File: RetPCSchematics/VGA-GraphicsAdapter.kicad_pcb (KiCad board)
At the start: 2 copper layers, 183.4 x 101.3 mm, 45 parts, among them J1 Bus_ISA_8bit, J2 74320-9004, U1 74AUC2G125, U10 ATmega644P-20PU, U11 628128, U12 628128, U13 SN74LVC245AN, U14 74LS245, U15 74LVC2G240, U16 74LVC2G240, U17 74LVC1G18, U18 74LVC1G18, U19 74LVC1G18, U2 74LVC2G240, U20 74LVC1G18, U21 ATF22V10D, U22 74LS245, U23 74LVC1G373, U24 74LVC1G373, U25 74LVC1G373, U26 74LVC1G373, U27 74LVC1G373, U28 74LVC1G373, U29 74LVC1G373, U3 ATF22V10D, U30 74LVC1G373, U31 74LVC1G373, U32 74LVC1G373, U33 74LVC1G373, U34 74LVC1G373, U37 ATF22V10D, U4 ATF22V10D, U5 74LS245, U6 ATF22V10D, U7 74LS245, U8 74LS245, U9 74LS245, X1 DGOF5S3

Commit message: sync
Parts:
- removed R1: 4.7k, Resistor_THT:R_Axial_DIN0411_L9.9mm_D3.6mm_P5.08mm_Vertical
- removed R2, R3, R4, R5, R6, R7: 4.7k, Resistor_THT:R_Axial_DIN0411_L9.9mm_D3.6mm_P7.62mm_Vertical
- added RN1: R_Network08, Resistor_THT:R_Array_SIP9, F.Cu at (153.2, 62.5)
- added U36: TFP410, retsmd:HQFP-64_10x10mm_Pitch0.5mm_handsoldering, F.Cu at (225.0, 84.6)
- U11, U12: footprint Package_DIP:DIP-24_W7.62mm_Socket -> SMD_Packages:SOJ-32
- U37: value ATF22V10D -> ATF750C
- moved U28 338.2 mm to (55.5, 20.9)
- moved U29 338.2 mm to (55.5, 13.6)
- moved U30 338.2 mm to (55.5, 17.3)
- moved U19 328.7 mm to (69.8, 22.4)
- moved U2 328.7 mm to (69.6, 25.5)
- moved U20 328.7 mm to (64.9, 26.1)
- moved U24 328.7 mm to (64.9, 22.5)
- moved U26 326.2 mm to (77.3, 9.75)
- moved U31 326.2 mm to (77.3, 13.4)
- moved U33 326.2 mm to (77.3, 20.7)
- moved U34 326.2 mm to (77.3, 17.0)
- moved U23 321.3 mm to (55.6, 27.9)
- moved U25 315.6 mm to (45.2, 29.0)
- moved U5 265.5 mm to (87.4, 78.7)
- moved U13 172.7 mm to (186.7, 13.5)
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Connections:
- U7 pad 2: /A15 -> /A8
- U7 pad 3: /A14 -> /A9
- U7 pad 4: /A13 -> /A10
- U7 pad 5: /A12 -> /A11
- U7 pad 6: /A11 -> /A12
- U7 pad 7: /A10 -> /A13
- U7 pad 8: /A9 -> /A14
- U7 pad 9: /A8 -> /A15
- U9 pad 2: /A7 -> /A0
- U9 pad 3: /A6 -> /A0
- U9 pad 4: /A5 -> /A0
- U9 pad 7: /A0 -> /A5
- U9 pad 8: /A0 -> /A6
- U9 pad 9: /A0 -> /A7
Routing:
- net (no net): track 423.5 -> 0.00 mm, vias 16 -> 0
- net /A0: track 0.00 -> 314.4 mm, vias 0 -> 6
- net /A6: track 0.00 -> 64.5 mm, vias 0 -> 1
- net /A8: track 0.00 -> 63.0 mm, vias 0 -> 1
- net /A5: track 0.00 -> 60.8 mm, vias 0 -> 1
- net /A7: track 0.00 -> 60.2 mm, vias 0 -> 1
- net /A9: track 0.00 -> 45.9 mm
- net /A13: track 0.00 -> 45.9 mm
- net /A12: track 0.00 -> 45.9 mm
- net /A10: track 0.00 -> 45.9 mm
- net /A11: track 0.00 -> 45.9 mm
- net /A14: track 0.00 -> 45.7 mm
- net /A15: track 0.00 -> 45.7 mm
- net Net-(U10-Pad15): track 0.00 -> 38.4 mm
- net Net-(U10-Pad16): track 0.00 -> 37.8 mm
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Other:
- board text removed: "VRAM"

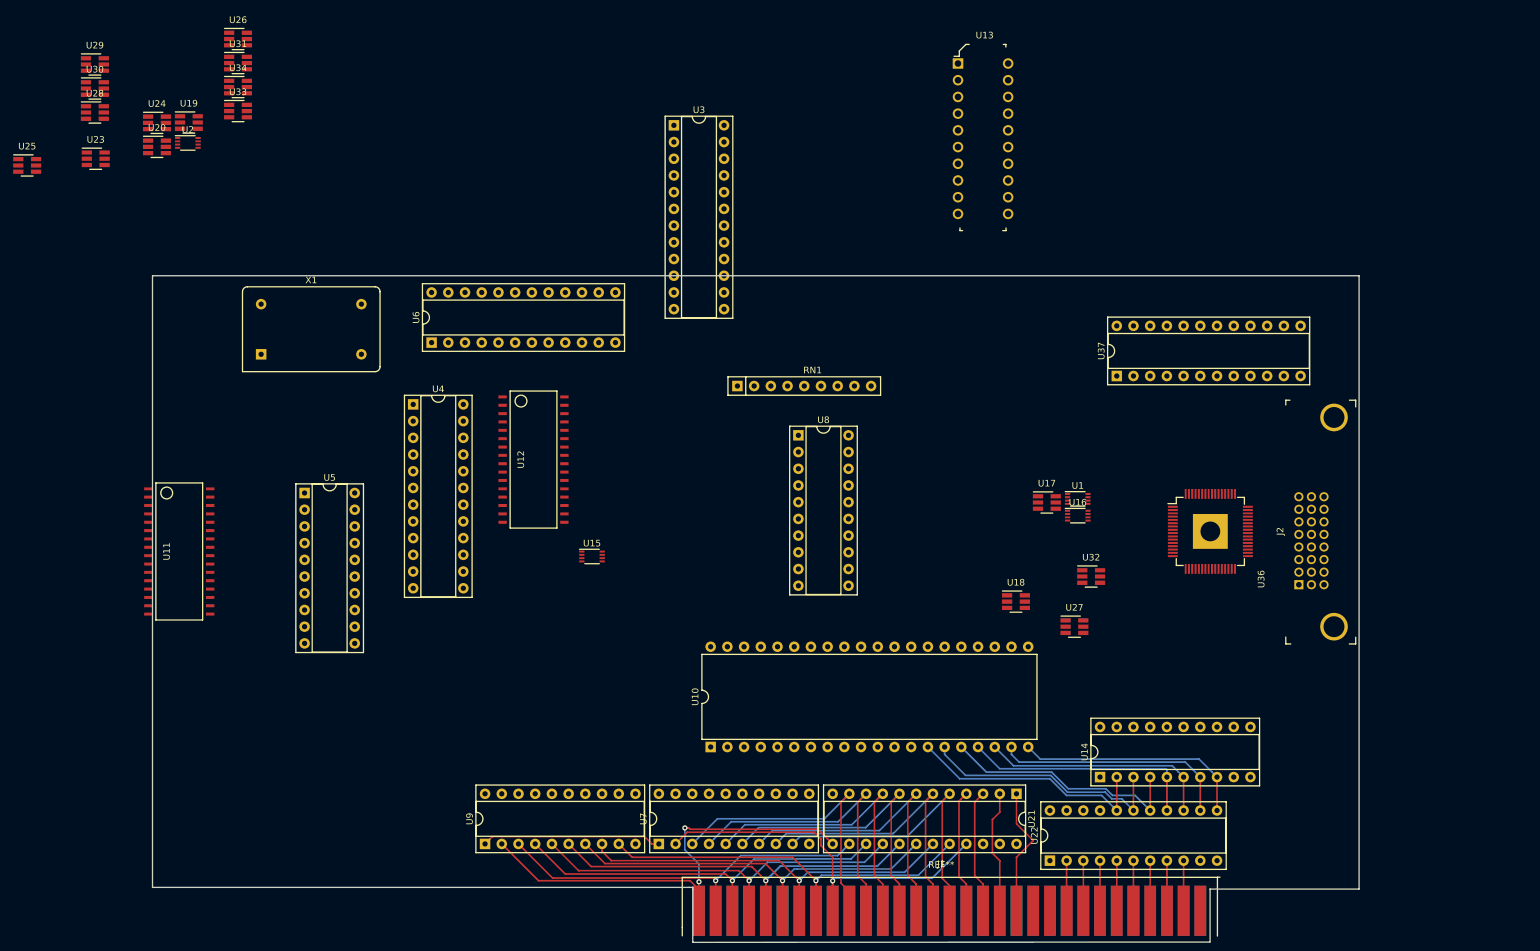
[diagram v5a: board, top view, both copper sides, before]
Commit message: Routed 2/3 of adapter and sync
sync and routed circuit a bit more
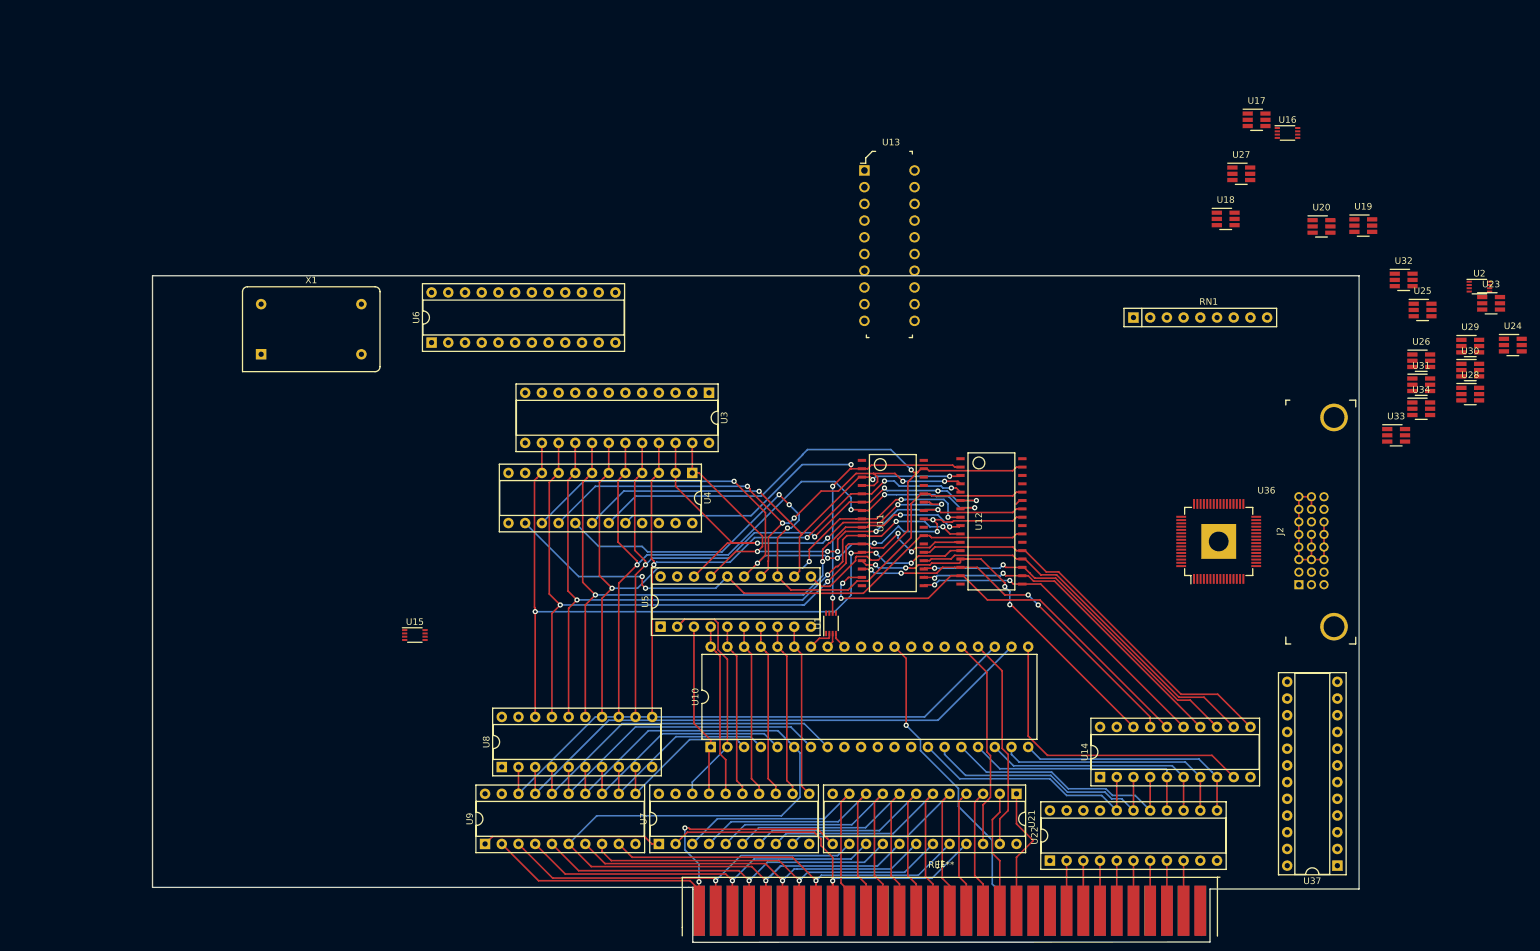
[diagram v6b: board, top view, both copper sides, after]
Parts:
- moved U28 213.4 mm to (264.5, 63.7)
- moved U29 213.4 mm to (264.5, 56.4)
- moved U30 213.4 mm to (264.5, 60.1)
- moved U25 213.2 mm to (257.3, 50.9)
- moved U23 213.2 mm to (267.7, 49.9)
- moved U24 208.8 mm to (271.0, 56.3)
- moved U2 197.5 mm to (265.9, 47.4)
- moved U26 186.4 mm to (257.1, 58.6)
- moved U31 186.4 mm to (257.1, 62.3)
- moved U34 186.4 mm to (257.1, 65.9)
- moved U33 182.8 mm to (253.3, 70.0)
- moved U19 179.2 mm to (248.3, 38.1)
- moved U20 177.4 mm to (241.9, 38.2)
- moved U11 108.5 mm to (176.8, 83.3)
- moved U37 81.6 mm to (244.3, 135.4), turned to 180 degrees
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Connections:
- U1 pad 2: /A17 -> /A16
- U1 pad 3: /A16 -> /A17
- U1 pad 5: /A16 -> /A17
- U1 pad 6: /A17 -> /A16
- U10 pad 1: Net-(U10-Pad1) -> /A9
- U10 pad 2: Net-(U10-Pad2) -> /A8
- U10 pad 24: REG -> Sel
- U10 pad 25: Sel -> REG
- U10 pad 3: Net-(U10-Pad3) -> /A7
- U10 pad 33: Net-(U10-Pad33) -> /A17
- U10 pad 34: Net-(U10-Pad34) -> /A16
- U10 pad 35: Net-(U10-Pad35) -> /A15
- U10 pad 36: Net-(U10-Pad36) -> /A14
- U10 pad 37: Net-(U10-Pad37) -> /A13
- U10 pad 38: Net-(U10-Pad38) -> /A12
- U10 pad 39: Net-(U10-Pad39) -> /A11
- U10 pad 4: Net-(U10-Pad4) -> /A6
- U10 pad 40: /A17 -> /A10
- U10 pad 5: Net-(U10-Pad5) -> /A5
- U10 pad 6: Net-(U10-Pad6) -> /A0
- U10 pad 7: Net-(U10-Pad7) -> /A0
- U10 pad 8: Net-(U10-Pad8) -> /A0
- U14 pad 11: Net-(U14-Pad11) -> /D7
- U14 pad 12: Net-(U14-Pad12) -> /D6
- U14 pad 13: Net-(U14-Pad13) -> /D5
- U14 pad 14: Net-(U14-Pad14) -> /D4
- U14 pad 15: Net-(U14-Pad15) -> /D3
- U14 pad 16: Net-(U14-Pad16) -> /D2
- U14 pad 17: Net-(U14-Pad17) -> /D1
- U14 pad 18: Net-(U14-Pad18) -> /D0
- U5 pad 11: Net-(U5-Pad11) -> /A15
- U5 pad 12: Net-(U5-Pad12) -> /A14
- U5 pad 13: Net-(U5-Pad13) -> /A13
- U5 pad 14: Net-(U5-Pad14) -> /A12
- U5 pad 15: Net-(U5-Pad15) -> /A11
- U5 pad 16: Net-(U5-Pad16) -> /A10
- U5 pad 17: Net-(U5-Pad17) -> /A9
- U5 pad 18: Net-(U5-Pad18) -> /A8
- U5 pad 2: /A15 -> /A8
- U5 pad 3: /A14 -> /A9
- U5 pad 4: /A13 -> /A10
- U5 pad 5: /A12 -> /A11
- U5 pad 6: /A11 -> /A12
- U5 pad 7: /A10 -> /A13
- U5 pad 8: /A9 -> /A14
- U5 pad 9: /A8 -> /A15
- U7 pad 11: Net-(U7-Pad11) -> /A15
- U7 pad 12: Net-(U7-Pad12) -> /A14
- U7 pad 13: Net-(U7-Pad13) -> /A13
- U7 pad 14: Net-(U7-Pad14) -> /A12
- U7 pad 15: Net-(U7-Pad15) -> /A11
- U7 pad 16: Net-(U7-Pad16) -> /A10
- U7 pad 17: Net-(U7-Pad17) -> /A9
- U7 pad 18: Net-(U7-Pad18) -> /A8
- U8 pad 11: Net-(U8-Pad11) -> /A7
- U8 pad 12: Net-(U8-Pad12) -> /A6
- U8 pad 13: Net-(U8-Pad13) -> /A5
- U8 pad 14: Net-(U8-Pad14) -> /A0
- U8 pad 15: Net-(U8-Pad15) -> /A0
- U8 pad 16: Net-(U8-Pad16) -> /A0
- U8 pad 17: Net-(U8-Pad17) -> /A0
- U8 pad 18: /A7 -> /A0
- U8 pad 2: Net-(U8-Pad2) -> /A0
- U8 pad 3: /A6 -> /A0
- U8 pad 4: /A5 -> /A0
- U8 pad 7: /A0 -> /A5
- U8 pad 8: /A0 -> /A6
- U8 pad 9: /A0 -> /A7
- U9 pad 11: Net-(U9-Pad11) -> /A7
- U9 pad 12: Net-(U9-Pad12) -> /A6
- U9 pad 13: Net-(U9-Pad13) -> /A5
- U9 pad 14: Net-(U9-Pad14) -> /A0
- U9 pad 15: Net-(U9-Pad15) -> /A0
- U9 pad 16: Net-(U9-Pad16) -> /A0
- U9 pad 17: Net-(U9-Pad17) -> /A0
- U9 pad 18: Net-(U9-Pad18) -> /A0
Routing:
- net /A0: track 314.4 -> 1222.7 mm, vias 6 -> 26
- net /A5: track 60.8 -> 204.2 mm, vias 1 -> 5
- net /A6: track 64.5 -> 196.7 mm, vias 1 -> 6
- net /A13: track 45.9 -> 171.5 mm, vias 0 -> 3
- net /A15: track 45.7 -> 170.8 mm, vias 0 -> 1
- net /A11: track 45.9 -> 169.7 mm, vias 0 -> 7
- net /A7: track 60.2 -> 179.6 mm, vias 1 -> 5
- net /A10: track 45.9 -> 158.4 mm, vias 0 -> 2
- net /A12: track 45.9 -> 155.5 mm, vias 0 -> 5
- net /A8: track 63.0 -> 167.8 mm, vias 1 -> 5
- net /A9: track 45.9 -> 149.6 mm, vias 0 -> 5
- net /A14: track 45.7 -> 143.8 mm, vias 0 -> 3
- net /A16: track 0.00 -> 82.8 mm, vias 0 -> 3
- net /D2: track 0.00 -> 66.2 mm, vias 0 -> 2
- net /D7: track 0.00 -> 61.7 mm
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
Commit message: sync
workstation switch sync
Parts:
- moved U19 61.0 mm to (190.1, 56.4), turned to 90 degrees
- moved U17 58.3 mm to (185.0, 56.4), turned to 90 degrees
- moved U20 51.6 mm to (191.9, 50.7), turned to 90 degrees
- moved U18 43.1 mm to (186.4, 50.7), turned to 90 degrees
- moved U13 42.2 mm to (180.8, 71.1), turned to 90 degrees
- moved U29 13.2 mm to (275.7, 63.5)
- moved RN1 11.2 mm to (206.2, 60.7), turned to 180 degrees
- moved U2 5.12 mm to (262.3, 43.8)
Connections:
- U13 pad 2: /D0 -> /D7
- U13 pad 3: /D1 -> /D6
- U13 pad 4: /D2 -> /D5
- U13 pad 5: /D3 -> /D4
- U13 pad 6: /D4 -> /D3
- U13 pad 7: /D5 -> /D2
- U13 pad 8: /D6 -> /D1
- U13 pad 9: /D7 -> /D0
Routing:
- net /D0: track 54.7 -> 86.4 mm
- net /D2: track 66.2 -> 90.0 mm, vias 2 -> 3
- net /D1: track 55.4 -> 79.0 mm
- net /D3: track 49.0 -> 70.5 mm
- net /D4: track 52.4 -> 73.8 mm
- net /D5: track 55.0 -> 75.7 mm
- net /D6: track 58.7 -> 78.8 mm, vias 0 -> 1
- net /D7: track 61.7 -> 81.2 mm, vias 0 -> 1
- net Net-(RN1-Pad8): track 0.00 -> 12.3 mm
- net Net-(RN1-Pad7): track 0.00 -> 5.79 mm
- net Net-(RN1-Pad9): track 0.00 -> 5.72 mm
- net Net-(RN1-Pad6): track 0.00 -> 2.79 mm
- net Net-(RN1-Pad5): track 0.00 -> 2.79 mm
- net Net-(RN1-Pad4): track 0.00 -> 2.79 mm
- net Net-(RN1-Pad3): track 0.00 -> 2.79 mm
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
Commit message: -
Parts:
- moved U16 77.0 mm to (173.7, 68.3)
- moved U24 72.4 mm to (198.7, 52.3)
- moved U23 69.1 mm to (198.6, 48.5)
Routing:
- net Net-(U17-Pad6): track 0.00 -> 20.9 mm
- net Net-(U18-Pad6): track 0.00 -> 17.2 mm
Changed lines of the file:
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@@
-(kicad_pcb (version 20171130) (host pcbnew "(5.0.0)")
+(kicad_pcb (version 20171130) (host pcbnew 5.0.1+dfsg1-3~bpo9+1)
   (general
     (thickness 1.6)
     (drawings 13)
-    (tracks 1046)
+    (tracks 1058)
     (zones 0)
     (modules 40)
@@
   )
   (module Package_SO:VSSOP-8_2.3x2mm_P0.5mm (layer F.Cu)
-    (at 236.772001 24.019001)
+    (at 173.736 68.326)
     (descr "VSSOP-8 2.3x2mm Pitch 0.5mm")
     (tags "VSSOP-8 2.3x2mm Pitch 0.5mm")
@@
       (effects (font (size 1 1) (thickness 0.15)))
     )
-    (fp_text user %R (at 0 0) (layer F.Fab)
+    (fp_text user %R (at 2.495999 4.428999) (layer F.Fab)
       (effects (font (size 0.5 0.5) (thickness 0.1)))
     )
@@
   )
   (module Package_TO_SOT_SMD:SOT-23-6_Handsoldering (layer F.Cu)
-    (at 271.018 56.261)
+    (at 198.708 52.258)
     (descr "6-pin SOT-23 package, Handsoldering")
     (tags "SOT-23-6 Handsoldering")
@@
   )
   (module Package_TO_SOT_SMD:SOT-23-6_Handsoldering (layer F.Cu)
-    (at 267.716 49.911)
+    (at 198.628 48.514)
     (descr "6-pin SOT-23 package, Handsoldering")
     (tags "SOT-23-6 Handsoldering")
@@
   (segment (start 178.816 103.886) (end 177.038 102.108) (width 0.25) (layer F.Cu) (net 69))
   (segment (start 178.816 114.046) (end 178.816 103.886) (width 0.25) (layer F.Cu) (net 69))
+  (segment (start 185.486 49.323) (end 185.486 48.293) (width 0.25) (layer F.Cu) (net 86))
+  (segment (start 185.486 48.293) (end 186.08499 47.69401) (width 0.25) (layer F.Cu) (net 86))
+  (segment (start 186.08499 47.69401) (end 193.74401 47.69401) (width 0.25) (layer F.Cu) (net 86))
+  (segment (start 196.328 53.208) (end 196.088 52.968) (width 0.25) (layer F.Cu) (net 86))
+  (segment (start 197.358 53.208) (end 196.328 53.208) (width 0.25) (layer F.Cu) (net 86))
+  (segment (start 193.74401 47.69401) (end 196.088 50.038) (width 0.25) (layer F.Cu) (net 86))
+  (segment (start 196.088 52.968) (end 196.088 50.038) (width 0.25) (layer F.Cu) (net 86))
+  (segment (start 184.028 49.090998) (end 185.874998 47.244) (width 0.25) (layer F.Cu) (net 90))
+  (segment (start 184.028 55.085) (end 184.028 49.090998) (width 0.25) (layer F.Cu) (net 90))
+  (segment (start 194.028 47.244) (end 196.248 49.464) (width 0.25) (layer F.Cu) (net 90))
+  (segment (start 196.248 49.464) (end 197.278 49.464) (width 0.25) (layer F.Cu) (net 90))
+  (segment (start 185.874998 47.244) (end 194.028 47.244) (width 0.25) (layer F.Cu) (net 90))
   (segment (start 167.636 101.35) (end 167.636 100.102) (width 0.25) (layer F.Cu) (net 110))
   (segment (start 166.878 102.108) (end 167.636 101.35) (width 0.25) (layer F.Cu) (net 110))
